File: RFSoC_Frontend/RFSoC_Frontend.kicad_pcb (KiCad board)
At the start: 4 copper layers, 165.1 x 44.6 mm, 72 parts, among them J1 Conn_Coaxial, J10 LPAM-40-01.0-X-08-X-K-TR, J2 Conn_Coaxial, J3 Conn_Coaxial, J4 Conn_Coaxial, J5 Conn_Coaxial, J6 Conn_Coaxial, J7 Conn_Coaxial, J8 Conn_Coaxial, J9 LPAM-40-01.0-X-08-X-K-TR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

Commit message: current
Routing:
- net /FMC BANK 0 (ADC)/UTIL_3V3: track 0.00 -> 6.35 mm
- net /FMC BANK 1 (DAC)/VCC12_SW: track 0.00 -> 5.08 mm
- net /FMC BANK 1 (DAC)/UTIL_3V3: track 0.00 -> 5.08 mm
- net /FMC BANK 1 (DAC)/DAC_AVTT_BUS: track 0.00 -> 3.81 mm
- net ADC_B0_P: track 31.4 -> 30.6 mm
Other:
- board size 165.1 x 44.6 mm -> 164.9 x 44.6 mm

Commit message: updated to remove 'eyeballed' measurements
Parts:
- removed REF (x2): MountingHole_2.2mm_M2_DIN965_Pad, MountingHole:MountingHole_2.2mm_M2_DIN965_Pad
- added e1: MountingHole_2.2mm_M2_DIN965_Pad, MountingHole:MountingHole_2.2mm_M2_DIN965_Pad, F.Cu at (160.0, 80.0)
- added e2: MountingHole_2.2mm_M2_DIN965_Pad, MountingHole:MountingHole_2.2mm_M2_DIN965_Pad, F.Cu at (85.0, 80.0)
- moved J10 22.1 mm to (122.5, 80.4)
- moved R29 22.0 mm to (133.1, 93.6)
- moved C10 22.0 mm to (132.5, 98.9)
- moved R17 22.0 mm to (133.1, 97.1)
- moved R22 22.0 mm to (132.5, 95.4)
- moved C1 22.0 mm to (231.9, 99.4)
- moved C13 22.0 mm to (119.7, 98.8)
- moved C14 22.0 mm to (118.7, 98.8)
- moved C2 22.0 mm to (230.9, 99.4)
- moved C5 22.0 mm to (189.3, 98.6)
- moved C6 22.0 mm to (188.3, 98.6)
- moved G*** 22.0 mm to (83.0, 109.0)
- moved J1 22.0 mm to (232.9, 111.4)
- moved J2 22.0 mm to (218.2, 111.4)
- moved J3 22.0 mm to (190.3, 111.4)
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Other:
- board text added: "7mm Diameter"

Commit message: updates
updated 3d footprints
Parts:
- J1, J2, J3, J4, J5, J6, J7, J8: footprint Connector_Coaxial:SMA_Amphenol_132289_EdgeMount -> local:SMA_Amphenol_132289_EdgeMount
- U1, U2, U3, U4, U5, U6, U7, U8: footprint MINICIRCUITS:XFMR_TCM2-33WX+ -> local:XFMR_TCM2-33WX+

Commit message: updated design for fixes
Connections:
- J9 pad B05: /FMC BANK 0 (ADC)/ADCIO_05 -> /FMC BANK 0 (ADC)/ADCIO_04
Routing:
- net DAC_A1_N: track 31.7 -> 28.5 mm
- net DAC_A1_P: track 30.1 -> 27.3 mm
- net ADC_B0_N: track 32.2 -> 30.0 mm
- net ADC_B0_P: track 30.6 -> 28.8 mm
- net DAC_B1_N: track 32.1 -> 30.3 mm
- net DAC_B1_P: track 30.4 -> 29.1 mm
- net ADC_B1_N: track 15.8 -> 14.6 mm
- net ADC_A1_N: track 16.5 -> 15.4 mm
- net ADC_A0_P: track 27.4 -> 28.4 mm
- net ADC_B1_P: track 14.1 -> 13.2 mm
- net Net-(J7-Pad1): track 8.57 -> 7.67 mm
- net Net-(J3-Pad1): track 6.86 -> 7.68 mm
- net Net-(J4-Pad1): track 6.79 -> 7.42 mm
- net Net-(J8-Pad1): track 8.51 -> 7.94 mm
- net GND: vias 78 -> 77
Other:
- copper layers 4 -> 2
- board text added: "For use with PLL Reference clock on FPGA"

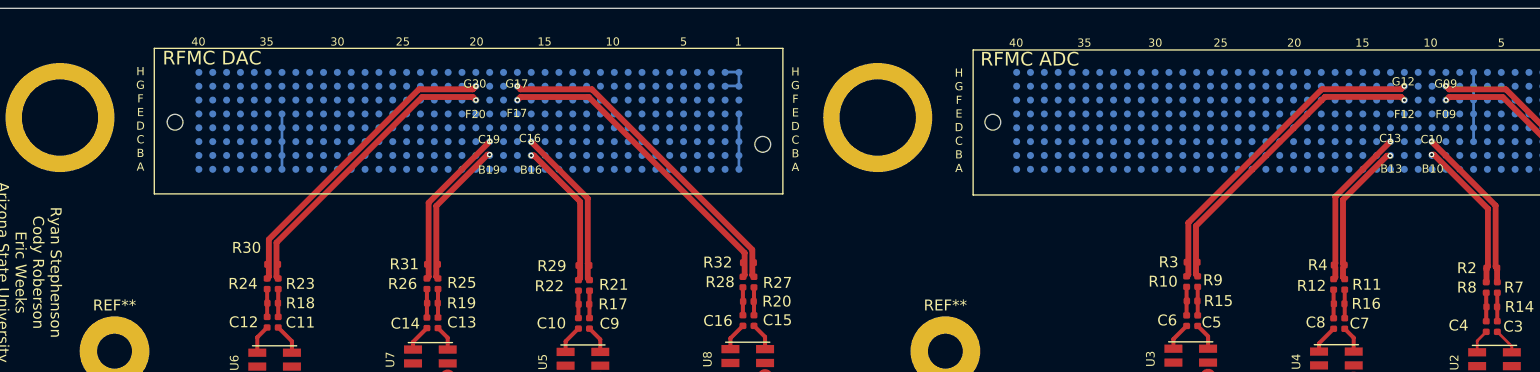
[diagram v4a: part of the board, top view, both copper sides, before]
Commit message: fixed grounded util 3v3 pins on the LPAM Cnctr
updated to REV B
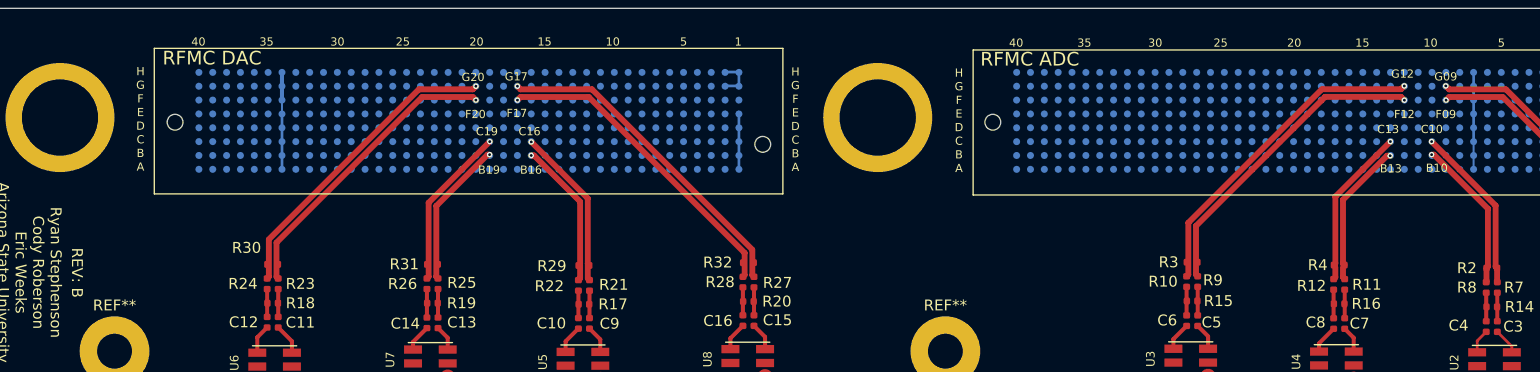
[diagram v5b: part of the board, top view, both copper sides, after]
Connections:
- J10 pad F34: GND -> /FMC BANK 1 (DAC)/UTIL_3V3
- J10 pad G34: GND -> /FMC BANK 1 (DAC)/UTIL_3V3
- J9 pad B07: GND -> /FMC BANK 0 (ADC)/UTIL_3V3
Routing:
- net /FMC BANK 1 (DAC)/UTIL_3V3: track 5.08 -> 8.89 mm
- net /FMC BANK 0 (ADC)/UTIL_3V3: track 6.35 -> 8.89 mm
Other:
- board text added: "REV: B"
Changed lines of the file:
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@@
   )
   (paper "A4")
+  (title_block
+    (title "RFSOC-RF-FRONTEND")
+    (date "2022-09-16")
+    (rev "B")
+    (company "ASU")
+    (comment 1 "Fixed grounded util-3v3pins g34, f34, b7 on the LPAM connector")
+  )
   (layers
     (0 "F.Cu" signal)
@@
       (net 34 "GND") (pinfunction "F33") (pintype "passive"))
     (pad "F34" smd circle locked (at 17.145 2.03 180) (size 0.64 0.64) (layers "B.Cu" "B.Mask")
-      (net 34 "GND") (pinfunction "F34") (pintype "passive"))
+      (net 141 "/FMC BANK 1 (DAC)/UTIL_3V3") (pinfunction "F34") (pintype "passive+no_connect"))
     (pad "F35" smd circle locked (at 18.415 2.03 180) (size 0.64 0.64) (layers "B.Cu" "B.Mask")
       (net 34 "GND") (pinfunction "F35") (pintype "passive"))
@@
       (net 34 "GND") (pinfunction "G33") (pintype "passive"))
     (pad "G34" smd circle locked (at 17.145 3.3 180) (size 0.64 0.64) (layers "B.Cu" "B.Mask")
-      (net 34 "GND") (pinfunction "G34") (pintype "passive"))
+      (net 141 "/FMC BANK 1 (DAC)/UTIL_3V3") (pinfunction "G34") (pintype "passive+no_connect"))
     (pad "G35" smd circle locked (at 18.415 3.3 180) (size 0.64 0.64) (layers "B.Cu" "B.Mask")
       (net 123 "unconnected-(J10-PadG35)") (pinfunction "G35") (pintype "passive+no_connect"))
@@
       (net 34 "GND") (pinfunction "B06") (pintype "passive"))
     (pad "B07" smd circle locked (at -17.145 -3.05 180) (size 0.64 0.64) (layers "B.Cu" "B.Mask")
-      (net 34 "GND") (pinfunction "B07") (pintype "passive"))
+      (net 64 "/FMC BANK 0 (ADC)/UTIL_3V3") (pinfunction "B07") (pintype "passive+no_connect"))
     (pad "B08" smd circle locked (at -15.875 -3.05 180) (size 0.64 0.64) (layers "B.Cu" "B.Mask")
       (net 34 "GND") (pinfunction "B08") (pintype "passive"))
@@
     (effects (font (size 0.75 0.75) (thickness 0.1875)))
   )
-  (gr_text "G20" (at 123.049984 76.904052) (layer "F.SilkS")
+  (gr_text "G20" (at 122.8852 76.3016) (layer "F.SilkS")
     (effects (font (size 0.75 0.75) (thickness 0.15)))
   )
@@
     (effects (font (size 0.75 0.75) (thickness 0.1875)))
   )
-  (gr_text "B10" (at 210.899984 84.704052) (layer "F.SilkS")
+  (gr_text "B10" (at 211.2772 84.6328) (layer "F.SilkS")
     (effects (font (size 0.75 0.75) (thickness 0.15)))
   )
@@
     (effects (font (size 0.75 0.75) (thickness 0.1875)))
   )
-  (gr_text "C13" (at 206.999984 81.904052) (layer "F.SilkS")
+  (gr_text "C13" (at 206.8068 81.0768) (layer "F.SilkS")
     (effects (font (size 0.75 0.75) (thickness 0.15)))
   )
@@
     (effects (font (size 0.75 0.75) (thickness 0.1875)))
   )
-  (gr_text "B13" (at 207.099984 84.704052) (layer "F.SilkS")
+  (gr_text "B13" (at 207.0608 84.6836) (layer "F.SilkS")
     (effects (font (size 0.75 0.75) (thickness 0.15)))
   )
@@
     (effects (font (size 1 1) (thickness 0.15)))
   )
-  (gr_text "G17" (at 126.899984 76.904052) (layer "F.SilkS")
+  (gr_text "G17" (at 126.8476 76.2508) (layer "F.SilkS")
     (effects (font (size 0.75 0.75) (thickness 0.15)))
   )
@@
     (effects (font (size 0.75 0.75) (thickness 0.1875)))
   )
-  (gr_text "C10" (at 210.799984 82.004052) (layer "F.SilkS")
+  (gr_text "C10" (at 210.82 81.0768) (layer "F.SilkS")
     (effects (font (size 0.75 0.75) (thickness 0.15)))
   )
@@
     (effects (font (size 0.75 0.75) (thickness 0.1875)))
   )
-  (gr_text "C19" (at 124.349984 82.004052) (layer "F.SilkS")
+  (gr_text "C19" (at 124.1552 81.28) (layer "F.SilkS")
     (effects (font (size 0.75 0.75) (thickness 0.15)))
   )
@@
     (effects (font (size 0.75 0.75) (thickness 0.1875)))
   )
-  (gr_text "G09" (at 212.099984 76.904052) (layer "F.SilkS")
+  (gr_text "G09" (at 212.099984 76.2508) (layer "F.SilkS")
     (effects (font (size 0.75 0.75) (thickness 0.15)))
   )
@@
     (effects (font (size 0.75 0.75) (thickness 0.1875)))
   )
-  (gr_text "C16" (at 128.099984 81.904052) (layer "F.SilkS")
+  (gr_text "C16" (at 128.0668 81.28) (layer "F.SilkS")
     (effects (font (size 0.75 0.75) (thickness 0.15)))
   )
@@
     (effects (font (size 0.75 0.75) (thickness 0.1875)))
   )
-  (gr_text "G12" (at 208.199984 76.704052) (layer "F.SilkS")
+  (gr_text "G12" (at 208.1276 75.9968) (layer "F.SilkS")
     (effects (font (size 0.75 0.75) (thickness 0.15)))
   )
+  (gr_text "REV: B" (at 86.5632 94.234 270) (layer "F.SilkS")
+    (effects (font (size 1 1) (thickness 0.15)))
+  )
   (gr_text "C" (at 152.449984 82.054052) (layer "F.SilkS")
     (effects (font (size 0.75 0.75) (thickness 0.1875)))
@@
   (via (at 126.9546 78.3998) (size 0.508) (drill 0.254) (layers "F.Cu" "B.Cu") (net 57))
   (segment (start 214.650032 75.860052) (end 214.650032 82.210052) (width 0.25) (layer "B.Cu") (net 64))
+  (segment (start 214.649678 82.210052) (end 214.649678 83.480052) (width 0.18288) (layer "B.Cu") (net 64))
+  (segment (start 214.649678 83.480052) (end 214.649678 84.750052) (width 0.18288) (layer "B.Cu") (net 64))
   (segment (start 147.270344 79.638052) (end 147.270344 84.718052) (width 0.25) (layer "B.Cu") (net 139))
   (segment (start 147.270344 77.098052) (end 146.000344 77.098052) (width 0.25) (layer "B.Cu") (net 140))
   (segment (start 146.000344 75.828052) (end 147.270344 75.828052) (width 0.25) (layer "B.Cu") (net 140))
   (segment (start 147.270344 75.828052) (end 147.270344 77.098052) (width 0.25) (layer "B.Cu") (net 140))
+  (segment (start 105.360026 75.860052) (end 105.360026 77.130052) (width 0.370586) (layer "B.Cu") (net 141))
+  (segment (start 105.360026 79.670052) (end 105.360026 78.400052) (width 0.18288) (layer "B.Cu") (net 141))
   (segment (start 105.360344 79.638052) (end 105.360344 84.718052) (width 0.25) (layer "B.Cu") (net 141))
+  (segment (start 105.360026 77.130052) (end 105.360026 78.400052) (width 0.370586) (layer "B.Cu") (net 141))
   (zone (net 0) (net_name "") (layer "F.Cu") (hatch edge 0.508)
     (connect_pads (clearance 0))
